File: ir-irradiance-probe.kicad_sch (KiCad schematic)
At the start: 5 parts, among them J2 SM04B-SRSS-TB-LF-SN, J3 PinHeader_1x2_P2.54mm_Drill1.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

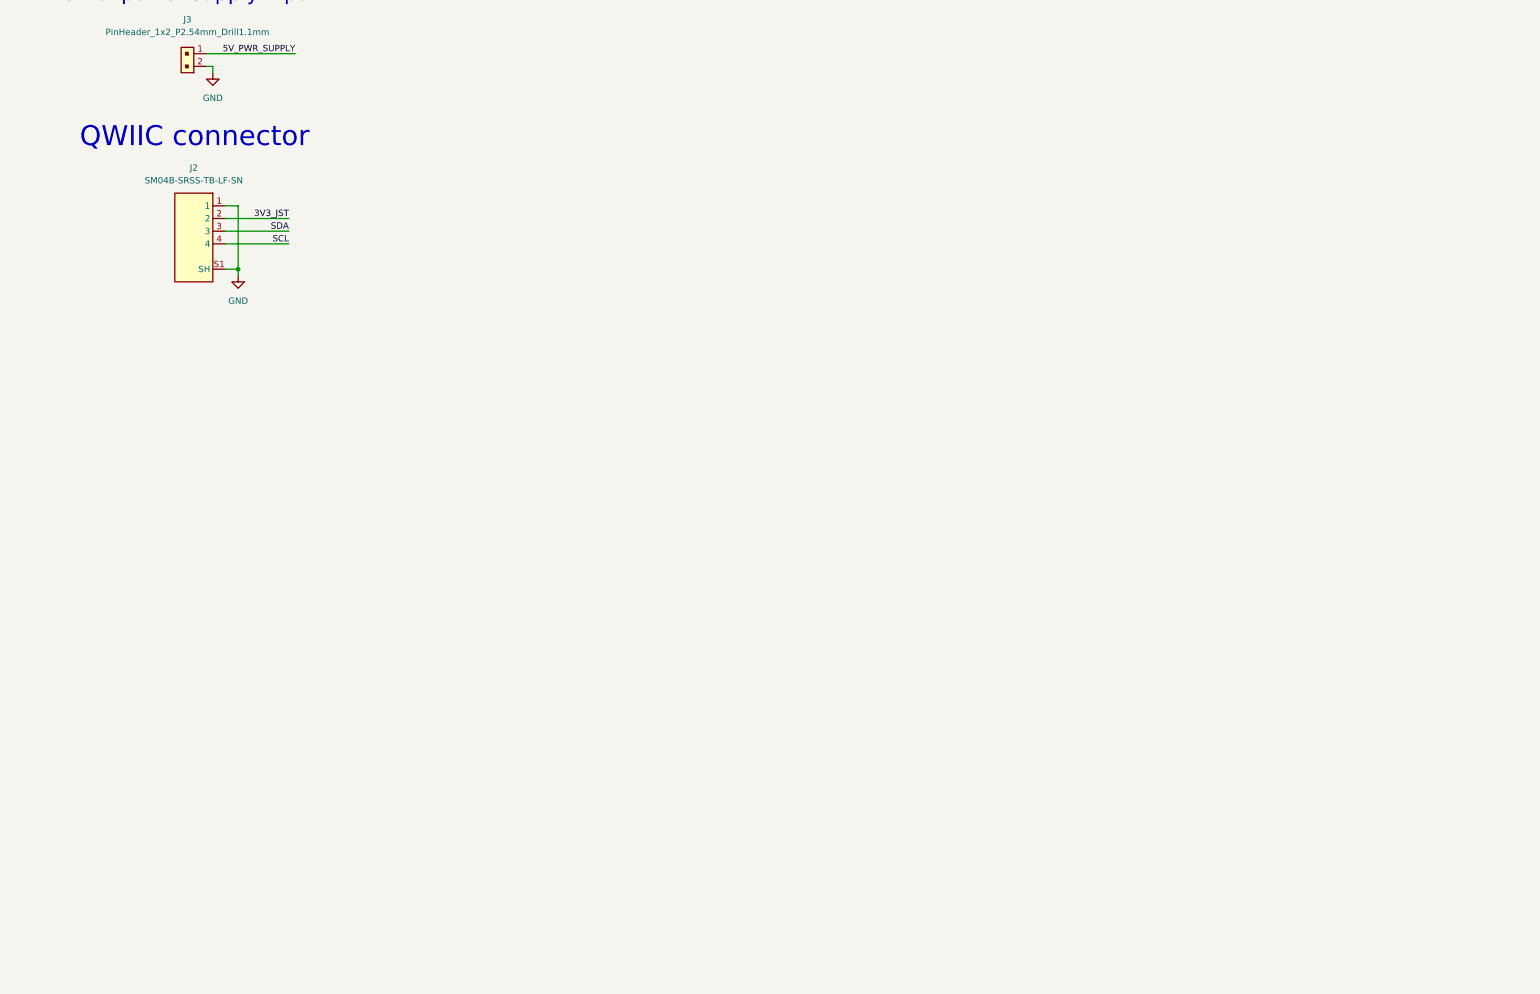
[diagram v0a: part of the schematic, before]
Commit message: [#47284] Add ADC and mounting holes on sch
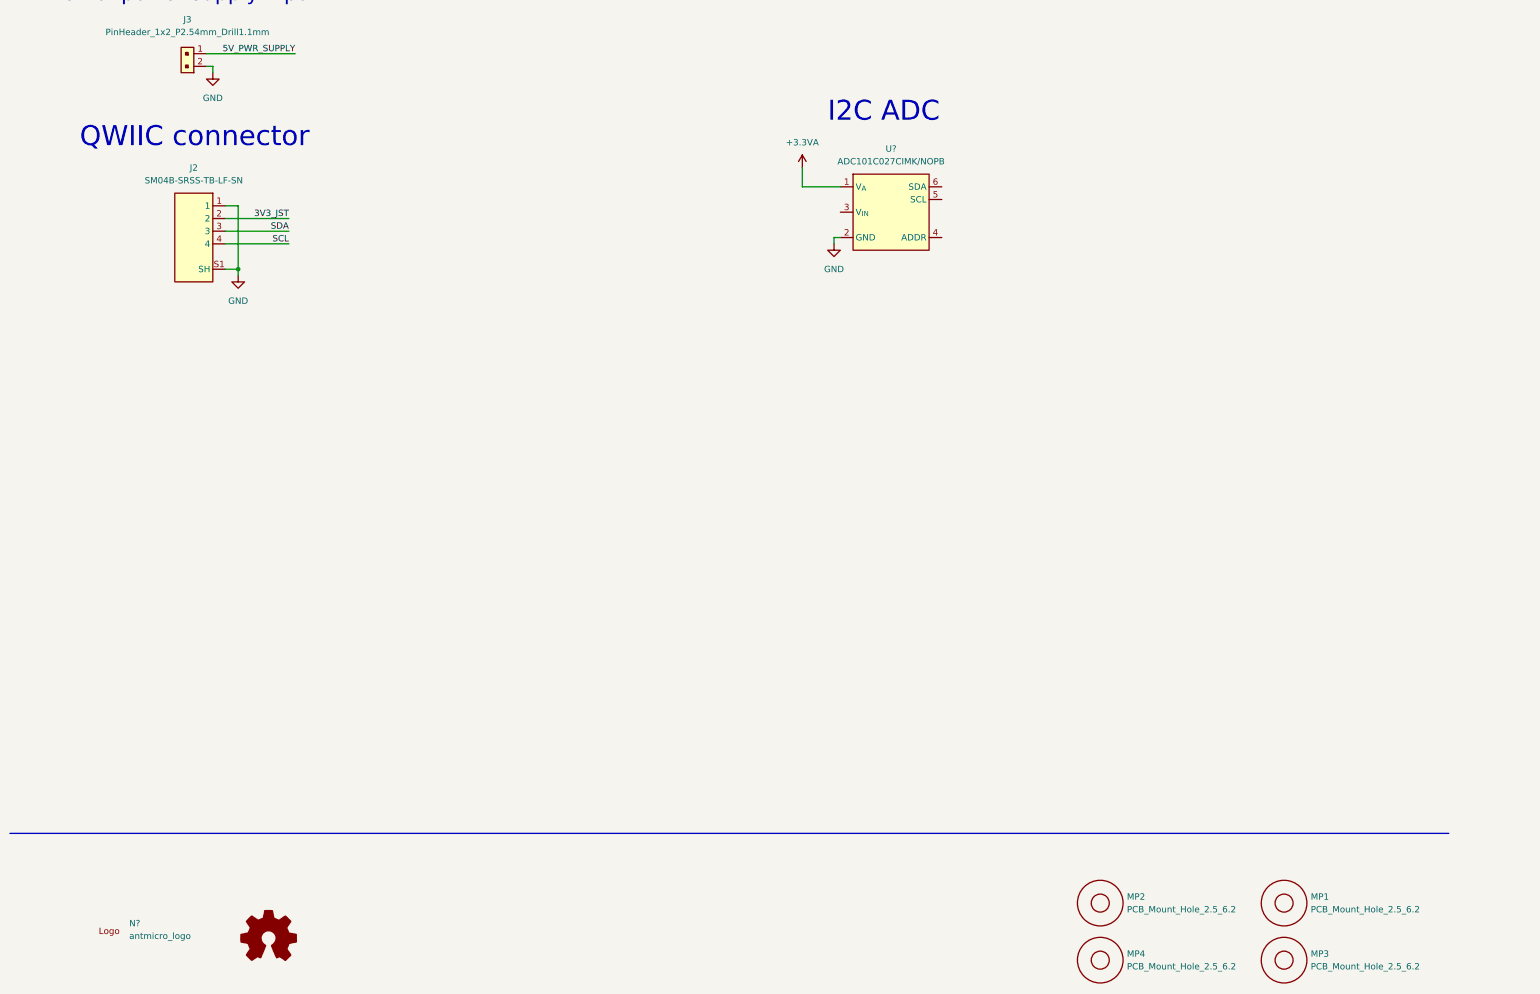
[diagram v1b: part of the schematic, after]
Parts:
- added MP1, MP2, MP3, MP4: PCB_Mount_Hole_2.5_6.2, antmicro-footprints:mounting-hole-2.75mm-M2.5_D6.2mm_PTH, symbol antmicroMechanicalParts:PCB_Mount_Hole_2.5_6.2
- added N?: antmicro_logo, antmicro-footprints:antmicro-logo, symbol antmicroMechanicalParts:antmicro_logo
- added U?: ADC101C027CIMK, antmicro-footprints:SOT-23-6, symbol antmicroDataAcquisitionAnalogtoDigitalConvertersADC:ADC101C027CIMK
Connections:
- net GND: now also U?.2 (GND)
- new net +3.3VA: U?.1 (V_{A})
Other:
- note added: "I2C ADC"

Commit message: [#47284] Add analog section to sch
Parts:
- added C? (x3): C, symbol Device:C
- added D? (x2): TEMD5020X01, antmicro-footprints:Photodiode_SMD_4.2x5mm_TEMD, symbol antmicroOpticalSensorsReflectiveAnalogOutput:TEMD5020X01
- added J?: Conn_BNC_031-70526-21, antmicro-footprints:Conn_BNC_031-70526-21, symbol antmicroCoaxialConnectorsRF:Conn_BNC_031-70526-21
- added POT? (x2): POT_20k_R0141-2-20k, antmicro-footprints:POT_R0141-2, symbol antmicroRotaryPotentiometersRheostats:POT_20k_R0141-2-20k
- added R? (x2): R_10k_0402, antmicro-footprints:R_0402_1005Metric, symbol antmicroResistors0402:R_10k_0402
- added R?: R_1k_0402, antmicro-footprints:R_0402_1005Metric, symbol antmicroResistors0402:R_1k_0402
- added R? (x2): R_47k_0402, antmicro-footprints:R_0402_1005Metric, symbol antmicroResistors0402:R_47k_0402
- added SW?: MSS3-V-T_R, antmicro-footprints:Switch_Slide_MSS3, symbol antmicroSlideSwitches:MSS3-V-T_R
- added U? (x5): AD8604ARUZ, antmicro-footprints:TSSOP-14_4.4x5mm_P0.65mm, symbol antmicroOperationalAmplifiers:AD8604ARUZ
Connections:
- net GND: now also C?.2, D?.1, D?.1, J?.2, U?.3 (+), U?.3 (+)
- net ADC_IR_SIG_IN: now reaches U?.3 (V_{IN})
- net ADC_IR_SIG_IN: now also U?.15 (-), U?.16
- new net: C?.1, D?.2, R?.1, R?.1, U?.2 (-) (x2)
- new net: POT?.1, R?.2 (x2)
- new net: J?.1, U?.6 (-), U?.7
- new net IR_900nm_OP_AMP_OUT: C?.2, C?.2, POT?.2, POT?.2, POT?.3, POT?.3, R?.2, R?.2, U?.1, U?.1
- new net SELECTED_IR_SIG: R?.1, U?.5 (+)
- new net SELECTED_IR_SIG_FILTERED: C?.1, R?.2, U?.14 (+)
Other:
- note added: "Analog buffer for ADC"
- note added: "BNC connector with analog buffer"
- note added: "Bottom IR 940nm with amplifier"
- note added: "Calculate value for 100kHz"
- note added: "Calculate value for 100kHz and mark as DNP"
- note added: "Cf = 1/(2pi * 47k * f), f=100kHz => Cf = 33pF"
- note added: "Find 100k potentiometer on DigiKey and replace this one"
- note added: "RC filter"
- note added: "Top IR 900nm with amplifier"

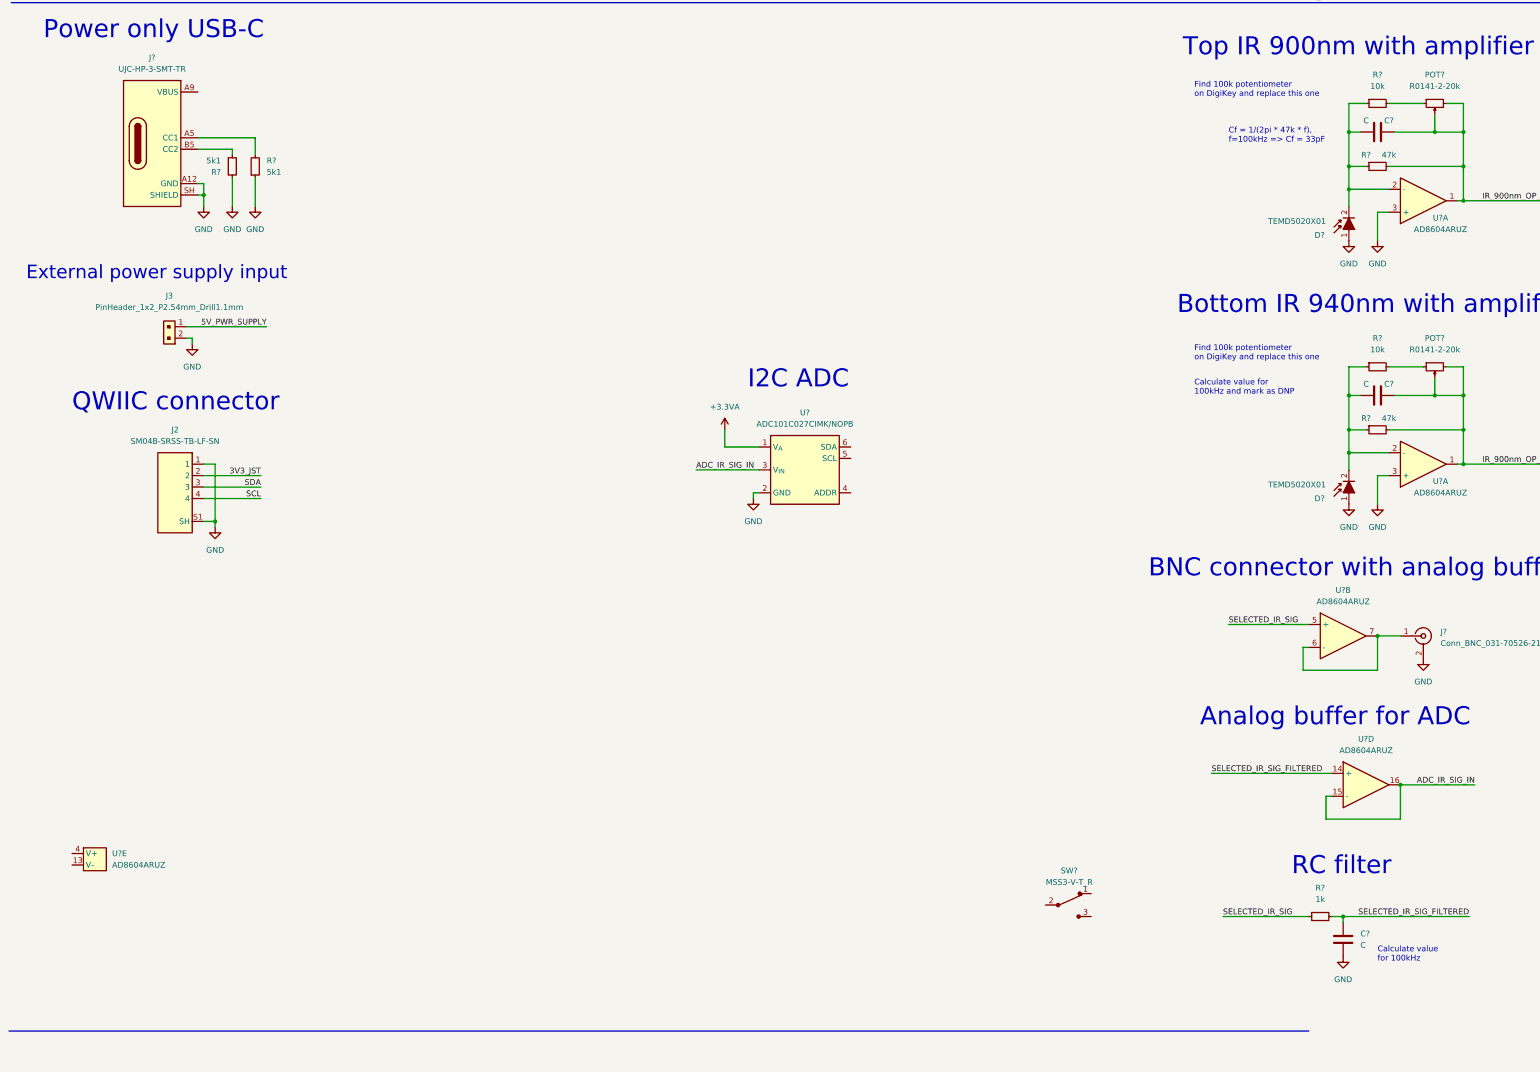
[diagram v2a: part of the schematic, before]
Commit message: [#47284] Add power section
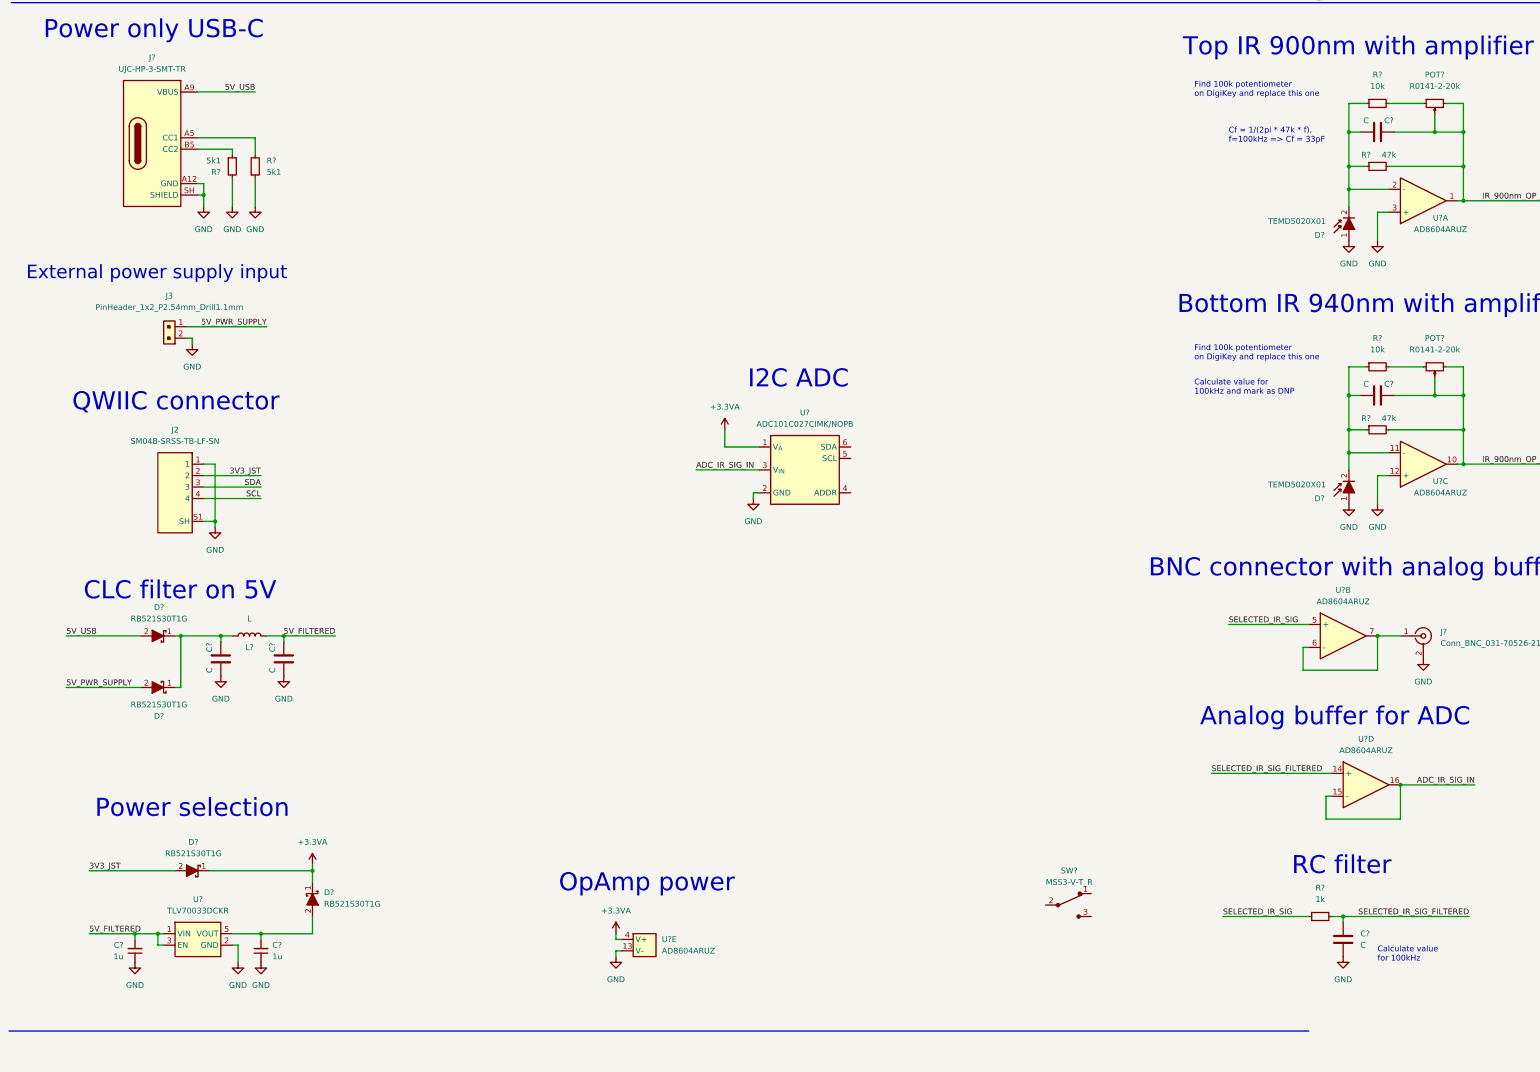
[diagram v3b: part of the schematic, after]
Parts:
- added C? (x2): C_1u_0402, antmicro-footprints:C_0402_1005Metric, symbol antmicroCapacitors0402:C_1u_0402
- added C? (x2): C, symbol Device:C
- added D? (x4): RB521S30T1G, antmicro-footprints:SOD-523, symbol antmicroDiodesRectifiersSingle:RB521S30T1G
- added L?: L, symbol Device:L
- added U?: TLV70033_SC70, antmicro-footprints:SC-70-5, symbol antmicroPMICVoltageRegulatorsLinear:TLV70033_SC70
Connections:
- net +3.3VA: now also U?.4 (V+), D?.1, D?.1
- net 3V3_JST: now also D?.2
- net 5V_PWR_SUPPLY: now also D?.2
- net GND: now also U?.12 (+), U?.13 (V-), C?.1, C?.1, C?.1, C?.1, U?.2 (GND); no longer U?.3 (+)
- net IR_900nm_OP_AMP_OUT: now also U?.10; no longer U?.1
- net at C?.1, D?.2, R?.1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: now also U?.11 (-); no longer U?.2 (-)
- net 5V_USB: now reaches J?.A9 (VBUS), J?.B9 (VBUS)
- net 5V_USB: now also D?.2
- new net: C?.2, D?.1, D?.1, L?.1
- new net: C?.2, D?.2, U?.5 (VOUT)
- new net 5V_FILTERED: C?.2, C?.2, L?.2, U?.1 (VIN), U?.3 (EN)
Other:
- note added: "CLC filter on 5V"
- note added: "OpAmp power"
- note added: "Power selection"
- moved on the sheet: U?E
